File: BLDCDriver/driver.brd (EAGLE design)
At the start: 42 x 49.1 mm, 66 parts, among them Q2 SIZ240DT-T1-GE3, Q3 SIZ240DT-T1-GE3, Q4 SIZ240DT-T1-GE3, U1 QFN50P400X400X100-25NDRV8300D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, U2 AS5048A-HTSP-500, U3 MCP2562-E/SN, U4 SOP80P620X125-8N, X2 JST-XH-06-PIN-LONG-PAD

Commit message: いい感じ🦀
# ==== Emojis ====
# ✨ :sparkles: Add new feature
# ✅  :white_check_mark: Update existing feature (not bug)
# ⚠️  :warning: Fix bug/error
# 🔥  :fire: Remove files or features
# ✏️ :pencil2: Fix typos
# 📝  :memo: Update documentation
# ♻️  :recycle: Dependencies update
# 🐧  :penguin: Improved the Linux
# 🍎  :apple: Improved the macOS
# 🔖 :bookmark: Add new library
# 🎉  :tada: Initial commit

# ==== Format ====
# :emoji: Subject
#
# Commit body...

# ==== Messages ====
# 新規(ファイル)機能追加: Add
# 機能修正、既存機能追加（バグではない): Update
# リファクタリング: Clean
# ファイル名変更:
# 削除など: Remove
# バグ修正: Fix
# バージョンアップ: Upgrade
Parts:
- moved BEAD 3.45 mm to (37.5, 39.5), turned to 90 degrees
- moved R21 2.22 mm to (39.5, 32.2)
- moved C7 1.27 mm to (33.0, 17.9)
- moved R2 1.27 mm to (8.73, 14.9)
- moved C1 1.27 mm to (13.7, 17.9)
- moved C5 1.27 mm to (11.9, 15.7)
- moved C6 1.27 mm to (31.3, 15.7)
- moved Q2 1.27 mm to (11.9, 15.2)
- moved Q4 1.27 mm to (31.3, 15.2)
- moved R1 1.27 mm to (15.1, 14.9)
- moved R11 1.27 mm to (29.5, 17.9)
- moved R14 1.27 mm to (10.2, 17.9)
- moved R6 1.27 mm to (28.1, 14.9)
- moved R5 1.27 mm to (34.4, 14.9)
- moved C14 0.79 mm to (24.8, 39.7)
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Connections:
- removed net V_CS: JP3.2
- net V: now also JP3.2
- net W: no longer JP3.3
- net W_CS: now also JP3.3
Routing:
- net GND: track 89.1 -> 179.4 mm, vias 21 -> 24
- net 3V3: track 2.53 -> 46.6 mm, vias 0 -> 5
- net 5V: track 0.00 -> 26.9 mm
- net PVDD: track 72.9 -> 92.4 mm
- net V: track 0.00 -> 17.3 mm
- net U_CS: track 3.62 -> 20.9 mm
- net SWDIO: track 0.00 -> 16.5 mm, vias 0 -> 1
- net GVDD: track 6.61 -> 22.6 mm
- net W_CS: track 0.00 -> 15.8 mm, vias 0 -> 1
- net SWCLK: track 0.00 -> 15.7 mm, vias 0 -> 1
- net LED: track 0.00 -> 14.5 mm, vias 0 -> 2
- net W: track 0.00 -> 10.4 mm
- net U: track 0.00 -> 9.72 mm
- net CANH: track 0.00 -> 8.30 mm, vias 0 -> 1
- net VDDA: track 0.00 -> 7.34 mm
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
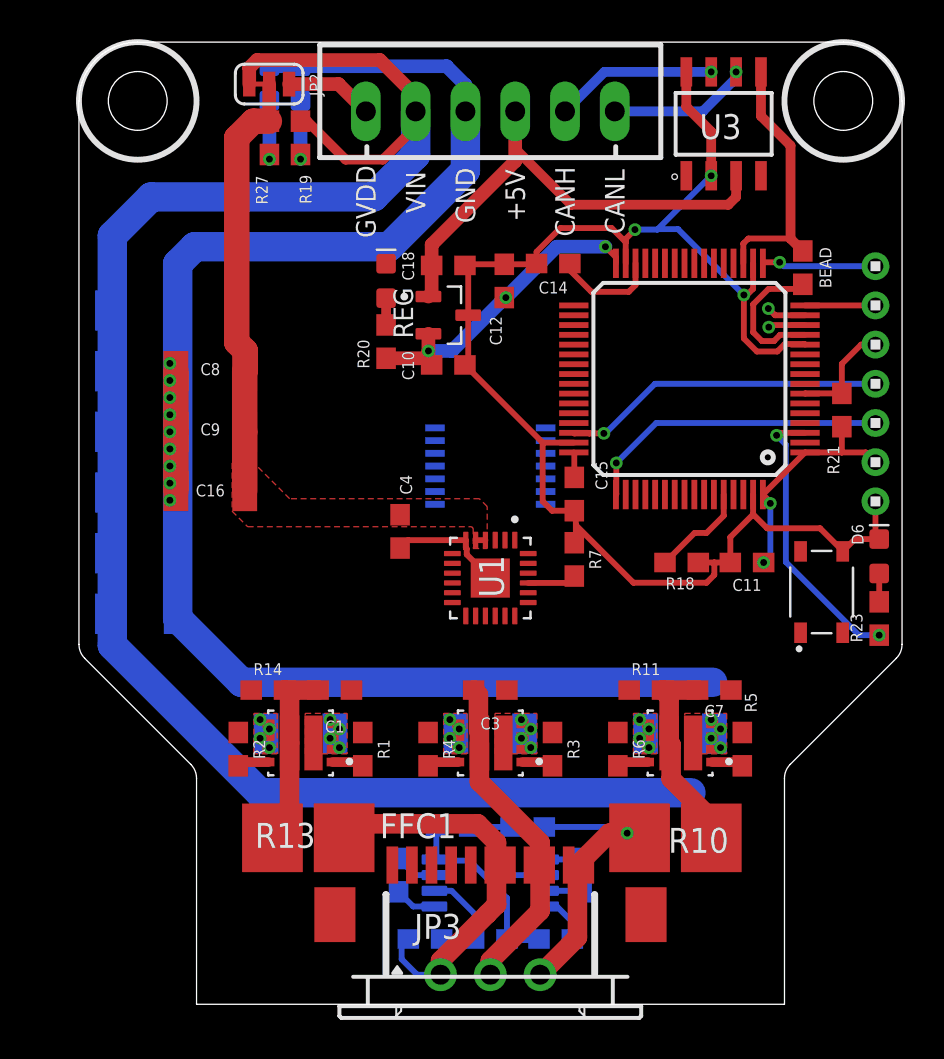
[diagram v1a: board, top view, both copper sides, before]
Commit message: ゲートドライバ周りの配線全部終わらせた
# ==== Emojis ====
# ✨ :sparkles: Add new feature
# ✅  :white_check_mark: Update existing feature (not bug)
# ⚠️  :warning: Fix bug/error
# 🔥  :fire: Remove files or features
# ✏️ :pencil2: Fix typos
# 📝  :memo: Update documentation
# ♻️  :recycle: Dependencies update
# 🐧  :penguin: Improved the Linux
# 🍎  :apple: Improved the macOS
# 🔖 :bookmark: Add new library
# 🎉  :tada: Initial commit

# ==== Format ====
# :emoji: Subject
#
# Commit body...

# ==== Messages ====
# 新規(ファイル)機能追加: Add
# 機能修正、既存機能追加（バグではない): Update
# リファクタリング: Clean
# ファイル名変更:
# 削除など: Remove
# バグ修正: Fix
# バージョンアップ: Upgrade
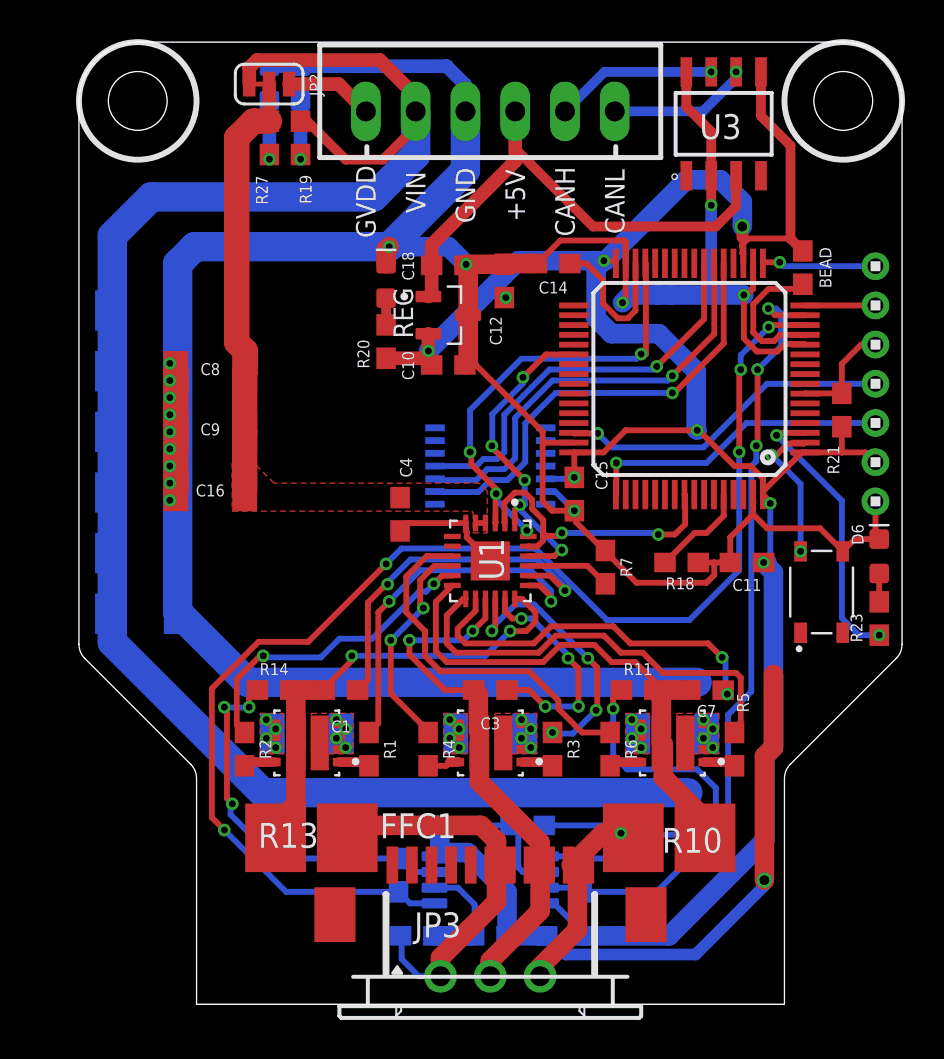
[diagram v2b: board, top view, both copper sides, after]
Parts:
- moved R7 1.64 mm to (27.5, 24.2)
- moved U1 0.87 mm to (21.6, 24.5)
- moved C4 0.87 mm to (17.0, 26.9)
- moved C34 0.43 mm to (25.3, 5.40)
- moved R15 0.43 mm to (17.9, 5.40)
- moved C6 0.40 mm to (30.9, 15.7)
- moved C7 0.40 mm to (32.6, 17.9)
- moved Q4 0.40 mm to (30.9, 15.2)
- moved R11 0.40 mm to (29.1, 17.9)
- moved R6 0.40 mm to (27.7, 14.9)
- moved R5 0.40 mm to (34.1, 14.9)
- moved C1 0.32 mm to (14.0, 17.9)
- moved C5 0.32 mm to (12.2, 15.7)
- moved Q2 0.32 mm to (12.2, 15.2)
- moved R2 0.32 mm to (9.05, 14.9)
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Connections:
- removed net HALL1: FFC1.3
- removed net HALL2: FFC1.4
- removed net HALL3: FFC1.2
- net 5V: no longer FFC1.1
- net GND: no longer FFC1.5
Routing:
- net C_U: track 4.06 -> 67.1 mm, vias 1 -> 5
- net 3V3: track 46.6 -> 109.6 mm, vias 5 -> 8
- net C_W: track 3.94 -> 40.7 mm, vias 1 -> 3
- net GND: track 179.4 -> 214.5 mm, vias 24 -> 28
- net INC: track 0.00 -> 24.0 mm, vias 0 -> 4
- net CLK: track 0.00 -> 23.1 mm, vias 0 -> 1
- net GHC: track 0.00 -> 22.3 mm
- net MISO: track 0.00 -> 22.2 mm, vias 0 -> 1
- net MOSI: track 0.00 -> 20.8 mm, vias 0 -> 1
- net BSTC: track 0.00 -> 19.0 mm, vias 0 -> 2
- net N$8: track 1.85 -> 20.6 mm, vias 0 -> 1
- net BSTA: track 0.00 -> 18.7 mm, vias 0 -> 2
- net GHA: track 0.00 -> 18.7 mm, vias 0 -> 2
- net GLC: track 0.00 -> 18.5 mm
- net N$10: track 2.18 -> 19.6 mm, vias 0 -> 3
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
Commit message: CANの配線をした
# ==== Emojis ====
# ✨ :sparkles: Add new feature
# ✅  :white_check_mark: Update existing feature (not bug)
# ⚠️  :warning: Fix bug/error
# 🔥  :fire: Remove files or features
# ✏️ :pencil2: Fix typos
# 📝  :memo: Update documentation
# ♻️  :recycle: Dependencies update
# 🐧  :penguin: Improved the Linux
# 🍎  :apple: Improved the macOS
# 🔖 :bookmark: Add new library
# 🎉  :tada: Initial commit

# ==== Format ====
# :emoji: Subject
#
# Commit body...

# ==== Messages ====
# 新規(ファイル)機能追加: Add
# 機能修正、既存機能追加（バグではない): Update
# リファクタリング: Clean
# ファイル名変更:
# 削除など: Remove
# バグ修正: Fix
# バージョンアップ: Upgrade
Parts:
- moved C4 1.19 mm to (18.2, 26.9)
- moved R7 0.50 mm to (27.9, 24.4)
- moved BEAD 0.24 mm to (37.8, 39.5)
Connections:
- net CANRX: now also NUCLEO_MAIN.PB9
- net CANTX: now also NUCLEO_MAIN.PB8
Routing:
- net GND: track 214.5 -> 256.3 mm, vias 28 -> 33
- net CANTX: track 0.00 -> 23.3 mm, vias 0 -> 4
- net CANRX: track 0.00 -> 18.5 mm, vias 0 -> 4
- net CS: track 0.00 -> 16.9 mm, vias 0 -> 1
- net PVDD: track 92.2 -> 102.9 mm
- net N$8: track 20.6 -> 28.0 mm
- net 3V3: track 109.6 -> 113.7 mm, vias 8 -> 9
- net INA: track 17.4 -> 21.1 mm
- net BSTA: track 18.7 -> 20.8 mm
- net INB: track 15.1 -> 16.9 mm
- net MISO: track 22.2 -> 20.6 mm
- net CLK: track 23.1 -> 21.6 mm
- net MOSI: track 20.8 -> 19.4 mm
- net SWCLK: track 15.7 -> 16.9 mm
- net BSTC: track 19.0 -> 17.8 mm
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
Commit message: 🔥完全体
1日寝かせる
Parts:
- moved C8 10.4 mm to (15.2, 27.5), turned to 90 degrees
- moved C16 4.80 mm to (12.1, 27.5), turned to 90 degrees
- moved C9 4.01 mm to (8.97, 27.5), turned to 90 degrees
- moved R6 1.11 mm to (26.6, 14.9)
- moved R4 0.95 mm to (17.5, 14.9)
- moved C1 0.56 mm to (13.9, 18.5)
- moved R14 0.56 mm to (10.5, 18.5)
- moved C7 0.48 mm to (32.6, 18.4)
- moved R11 0.48 mm to (29.1, 18.4)
- moved R2 0.40 mm to (8.65, 14.9)
- moved S1 0.32 mm to (38.5, 23.3)
- moved R7 0.24 mm to (28.2, 24.4)
- moved R18 0.16 mm to (31.5, 24.4)
- moved C11 0.08 mm to (34.8, 24.4)
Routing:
- net GVDD: track 22.6 -> 4.42 mm
- net GND: track 256.3 -> 240.6 mm, vias 33 -> 46
- net N$10: track 19.6 -> 28.1 mm, vias 3 -> 1
- net PVDD: track 102.9 -> 109.1 mm, vias 12 -> 34
- net GLC: track 18.5 -> 23.0 mm
- net BSTA: track 20.8 -> 18.4 mm
- net 3V3: track 113.7 -> 115.8 mm, vias 9 -> 10
- net BSTB: track 11.6 -> 9.75 mm, vias 4 -> 2
- net W: track 27.1 -> 28.6 mm
- net GHC: track 22.3 -> 23.6 mm
- net BSTC: track 17.8 -> 19.0 mm
- net C_U: track 67.0 -> 68.1 mm
- net LC: track 1.61 -> 2.73 mm
- net LB: track 1.61 -> 2.57 mm
- net N$11: track 7.01 -> 6.05 mm
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- added copper zone on layer 16, net GND
- added copper zone on layer 1, net GVDD_IN
- added copper zone on layer 16, net PVDD

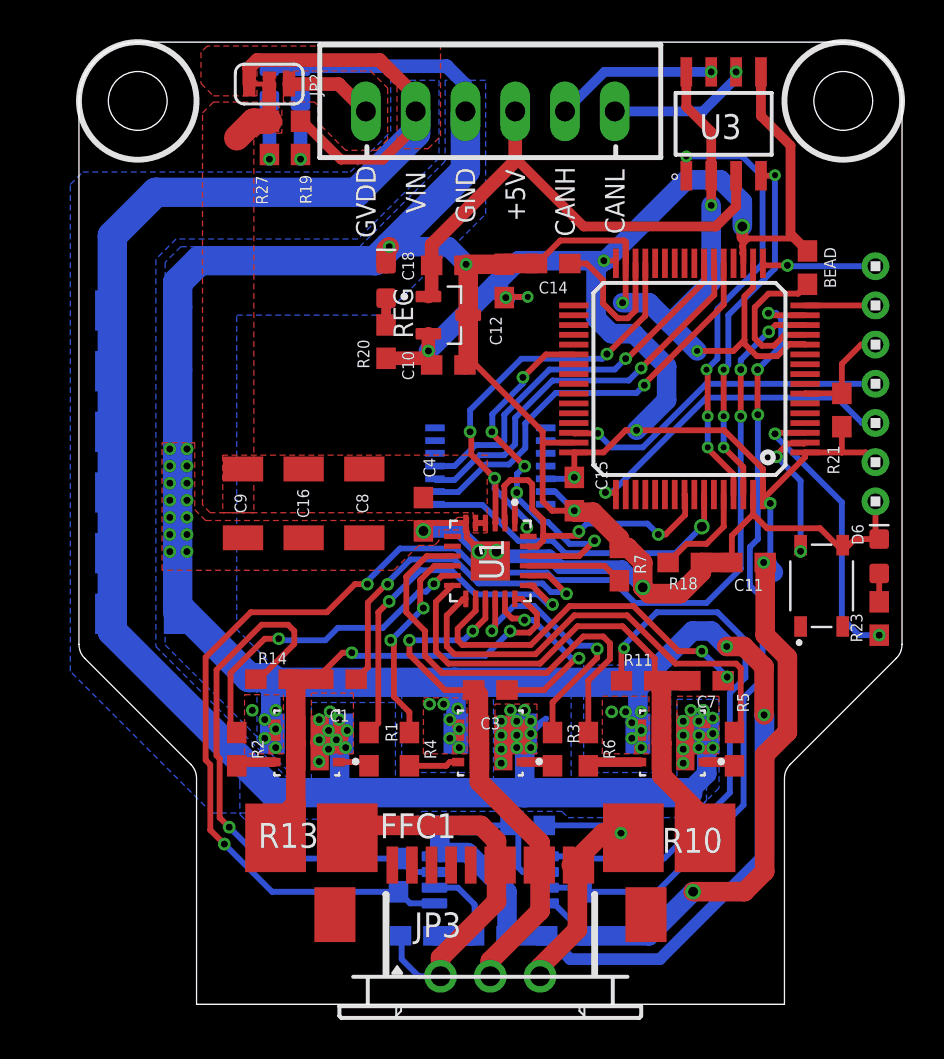
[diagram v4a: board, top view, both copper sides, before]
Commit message: 電源ラインのパワみを増やした
# ==== Emojis ====
# ✨ :sparkles: Add new feature
# ✅  :white_check_mark: Update existing feature (not bug)
# ⚠️  :warning: Fix bug/error
# 🔥  :fire: Remove files or features
# ✏️ :pencil2: Fix typos
# 📝  :memo: Update documentation
# ♻️  :recycle: Dependencies update
# 🐧  :penguin: Improved the Linux
# 🍎  :apple: Improved the macOS
# 🔖 :bookmark: Add new library
# 🎉  :tada: Initial commit

# ==== Format ====
# :emoji: Subject
#
# Commit body...

# ==== Messages ====
# 新規(ファイル)機能追加: Add
# 機能修正、既存機能追加（バグではない): Update
# リファクタリング: Clean
# ファイル名変更:
# 削除など: Remove
# バグ修正: Fix
# バージョンアップ: Upgrade
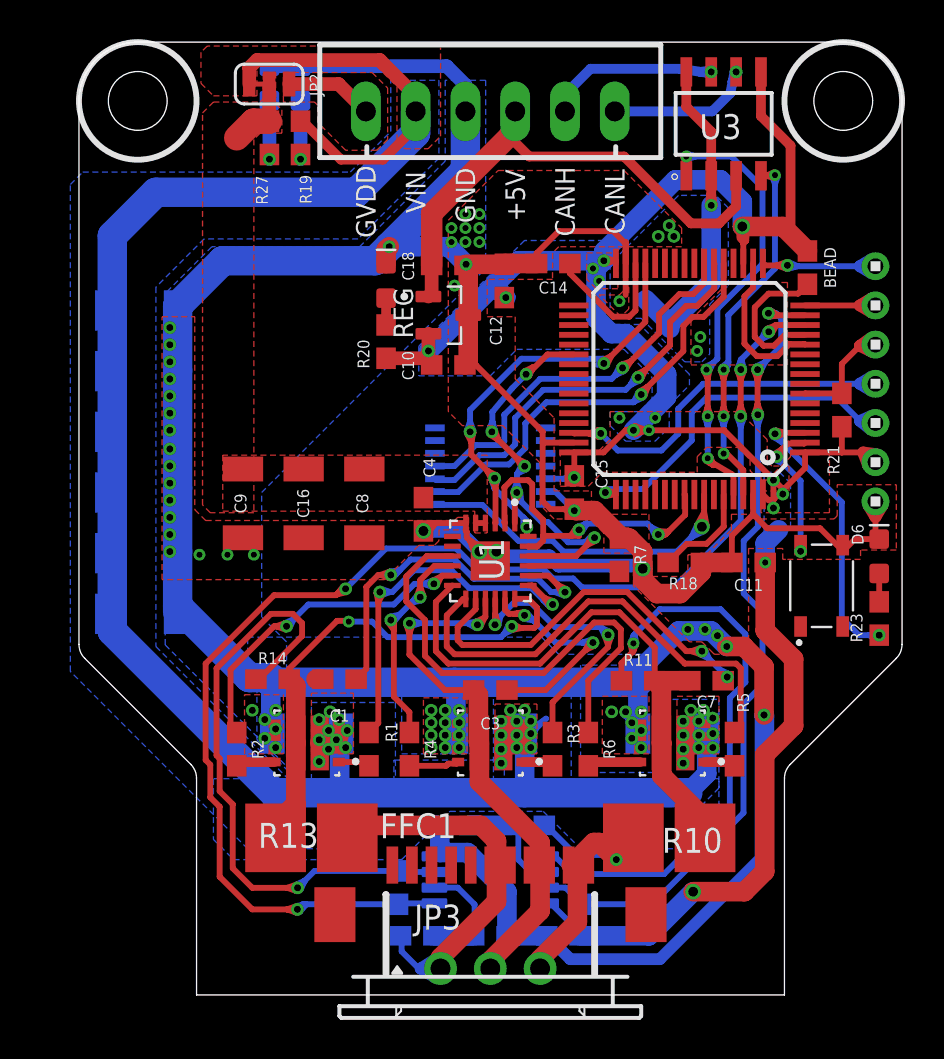
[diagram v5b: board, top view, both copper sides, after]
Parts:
- moved R16 0.63 mm to (16.9, 7.86)
- moved R8 0.63 mm to (26.3, 7.86)
- moved R7 0.48 mm to (28.2, 24.8)
- moved JP3 0.40 mm to (21.6, 3.73)
- moved C15 0.08 mm to (25.9, 28.0)
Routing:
- net GND: track 240.6 -> 261.8 mm, vias 46 -> 70
- net INA: track 21.1 -> 34.6 mm
- net 3V3: track 115.8 -> 128.1 mm, vias 10 -> 16
- net C_U: track 68.1 -> 79.2 mm
- net INC: track 23.6 -> 33.8 mm
- net C_W: track 40.8 -> 49.9 mm
- net CANTX: track 23.3 -> 31.6 mm
- net PVDD: track 109.1 -> 117.2 mm
- net CANRX: track 18.5 -> 25.7 mm
- net BSTB: track 9.75 -> 16.3 mm
- net GHA: track 18.5 -> 24.4 mm
- net GHB: track 13.8 -> 19.7 mm
- net N$10: track 28.1 -> 34.0 mm
- net SWCLK: track 16.9 -> 22.6 mm
- net BSTA: track 18.4 -> 23.9 mm
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- added copper zone on layer 1, net 3V3
- added copper zone on layer 16, net 3V3
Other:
- board size 42 x 49.1 mm -> 42 x 48.6 mm

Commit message: ⚡️電源周りの配線パワみ増した
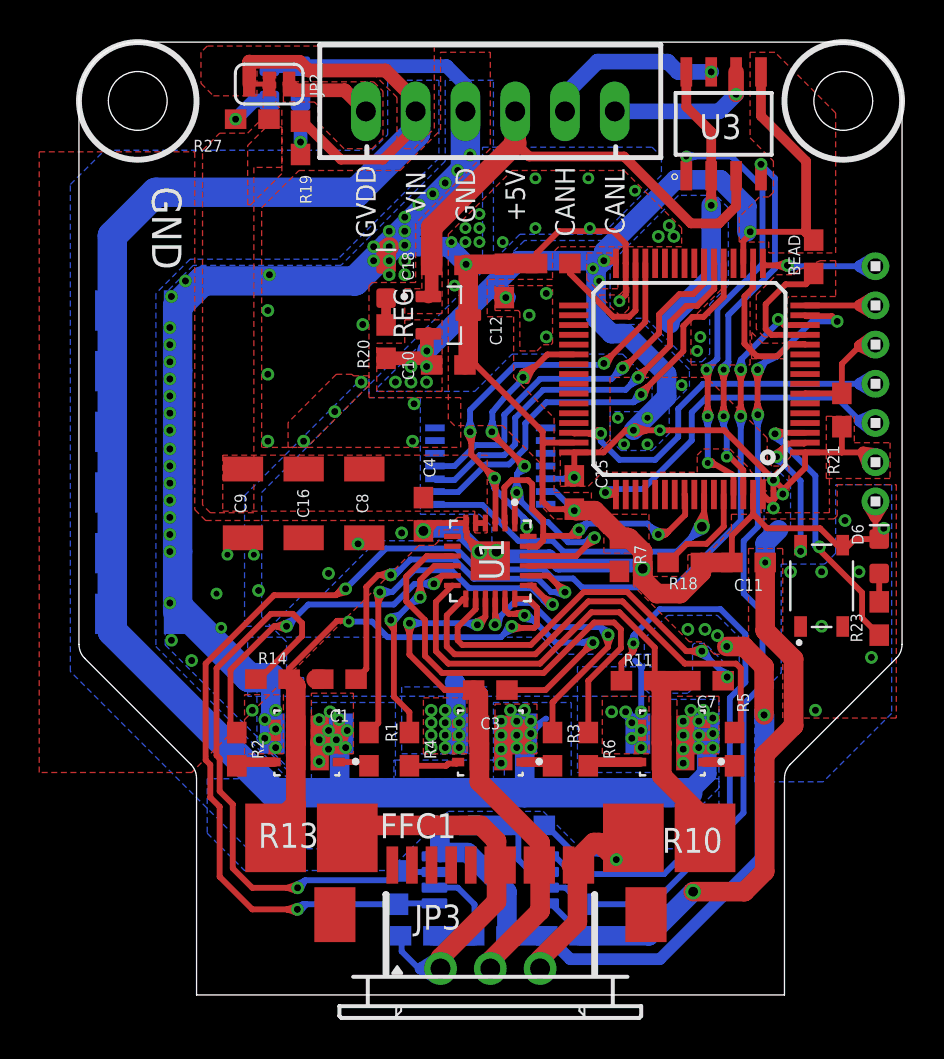
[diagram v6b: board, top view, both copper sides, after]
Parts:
- moved R27 1.29 mm to (9.45, 47.1), turned to 0 degrees
- moved BEAD 0.64 mm to (38.1, 40.0)
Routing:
- net GND: track 261.8 -> 234.2 mm, vias 70 -> 117
- net 3V3: track 128.1 -> 121.4 mm, vias 16 -> 27
- net GVDD: track 4.42 -> 0.60 mm
- net C_U: track 79.2 -> 76.9 mm
- net LED: track 18.7 -> 16.9 mm
- net CANRX: track 25.7 -> 24.0 mm
- net C_W: track 49.9 -> 48.2 mm
- net N$15: track 3.46 -> 2.12 mm
- net VDDA: track 7.67 -> 6.60 mm
- net CANL: track 8.65 -> 7.69 mm
- net INC: track 33.8 -> 32.9 mm
- net CANH: track 10.1 -> 9.24 mm
- net SWDIO: track 21.5 -> 22.2 mm
- net PVDD: track 117.2 -> 116.5 mm
- net INA: track 34.6 -> 35.3 mm
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- added copper zone on layer 1, net 5V
- added copper zone on layer 1, net VDDA

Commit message: CANトランシーバーの近くにコンデンサつけた
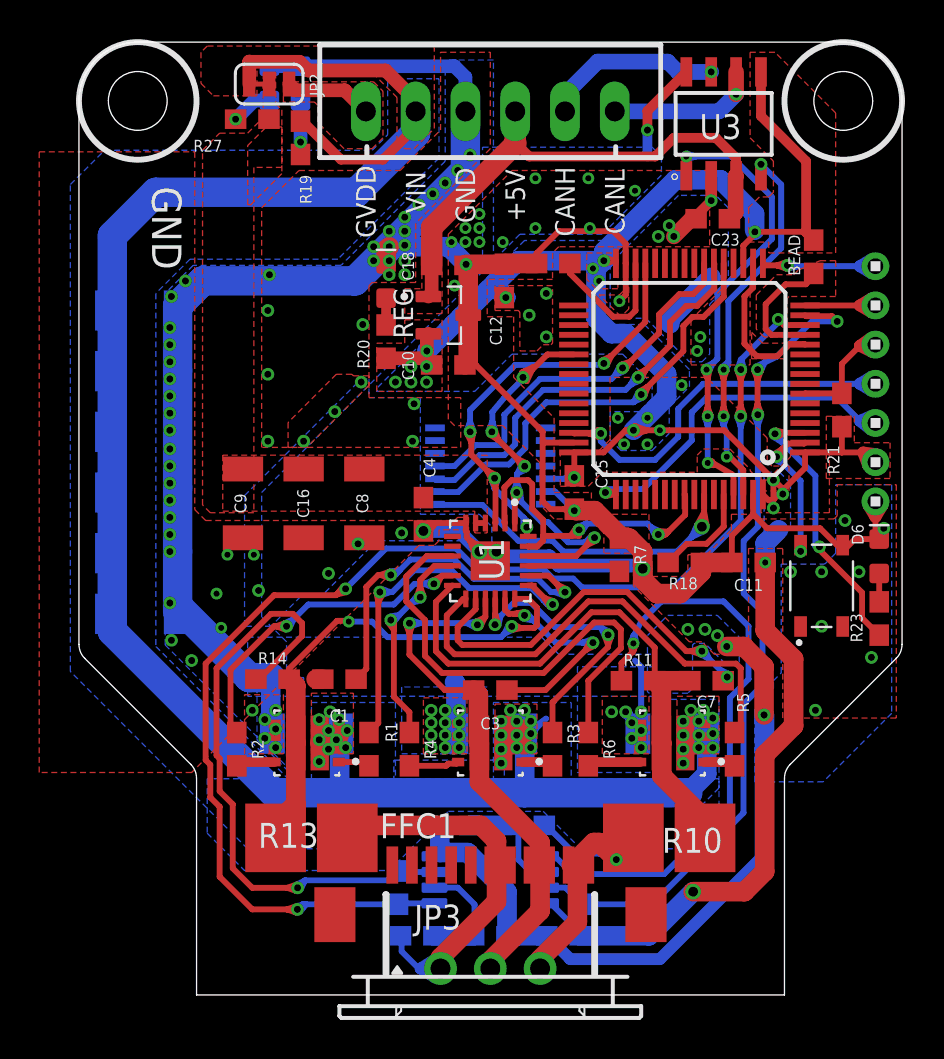
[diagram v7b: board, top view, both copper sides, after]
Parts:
- added C23: 0.1uF, SparkFun-Capacitors:0603
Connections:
- net 5V: now also C23.1
- net GND: now also C23.2
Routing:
- net GND: track 234.2 -> 231.4 mm, vias 117 -> 118
- net N$8: track 32.1 -> 33.0 mm
- net 5V: track 26.2 -> 26.9 mm
